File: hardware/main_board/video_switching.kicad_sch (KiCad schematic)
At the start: 33 parts, among them SW1 rgb/ypbpr, SW2 rgb/ypbpr, SW3 rgb/ypbpr, SW4 rgb/ypbpr, SW5 rgb/ypbpr, SW6 rgb/ypbpr, SW7 rgb/ypbpr, SW8 rgb/ypbpr, U10 SN74CBT3244CPW, U11 SN74CBT3244CPW, U12 SN74CBT3244CPW, U13 SN74CBT3244CPW, U14 74HC238, U15 74HC238, U3 SN74CBT3244CPW, U4 SN74CBT3244CPW, U5 74HC138, U6 74HC04, U7 SN74CBT3244CPW, U8 SN74CBT3244CPW, U9 SN74CBT3244CPW

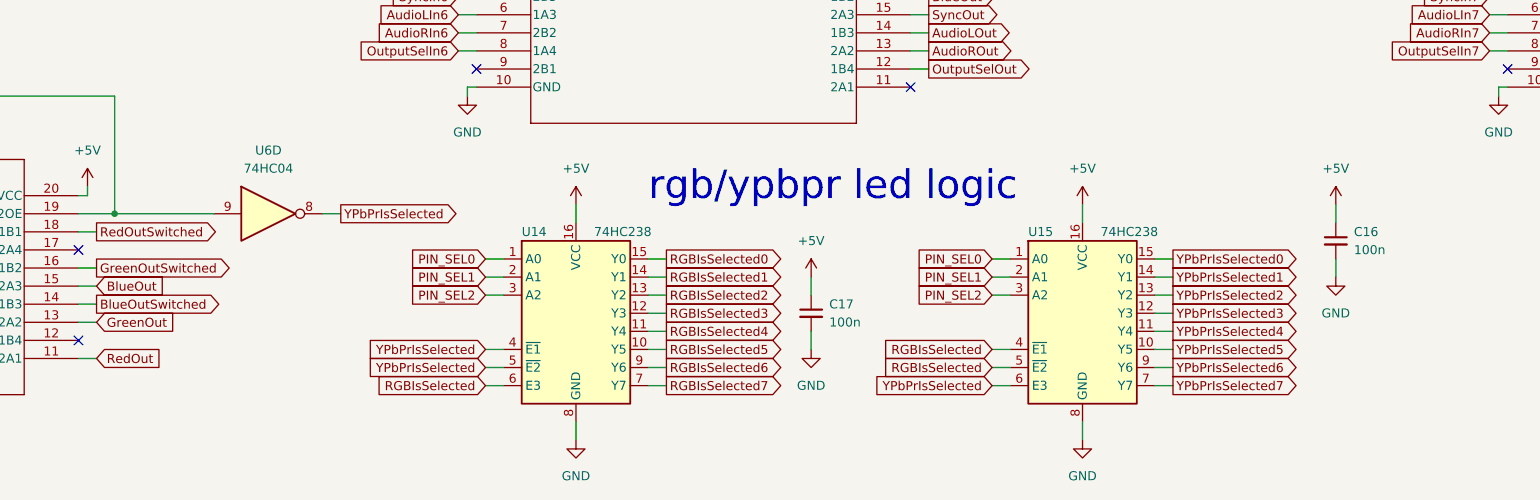
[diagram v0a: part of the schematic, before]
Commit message: #2: Hardware changes to accommodate new standby feature. Might as well commit symbol/footprint tables.
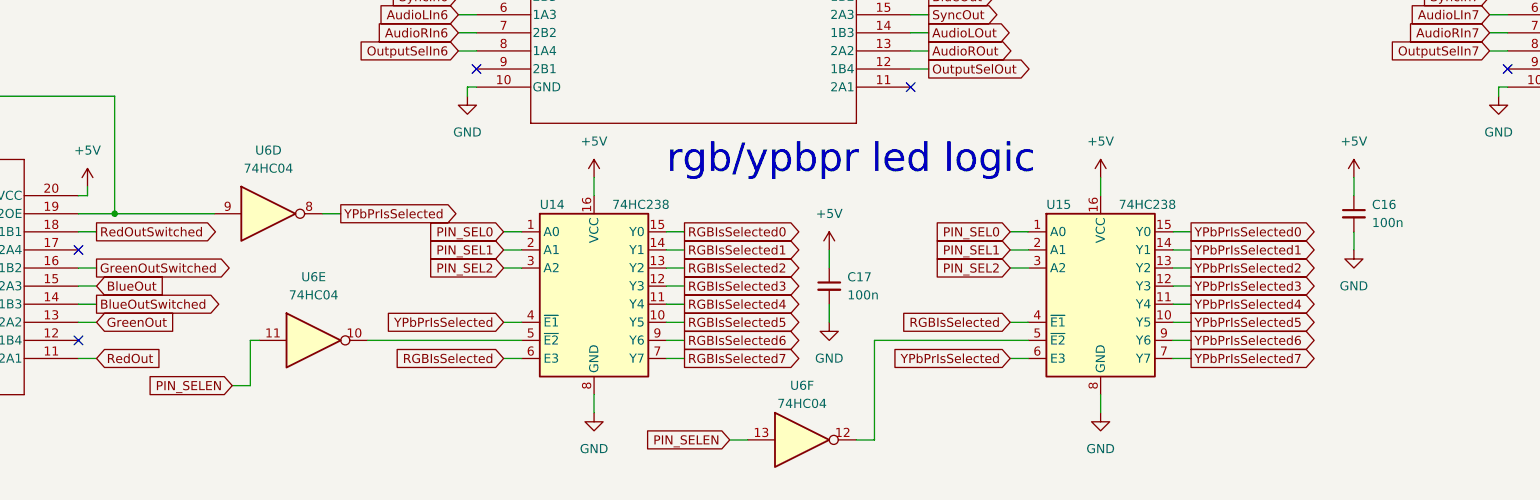
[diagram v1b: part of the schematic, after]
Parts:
- added unit 5 of U6
- added unit 6 of U6
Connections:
- net OutputSelOut: no longer U15.5 (~{E2})
- net PIN_SELEN: now also U6.11, U6.13
- net YPbPrIsSelected: no longer U14.5 (~{E2})
- new net: U14.5 (~{E2}), U6.10
- new net: U15.5 (~{E2}), U6.12
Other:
- moved on the sheet: C16, C17, U14, U15

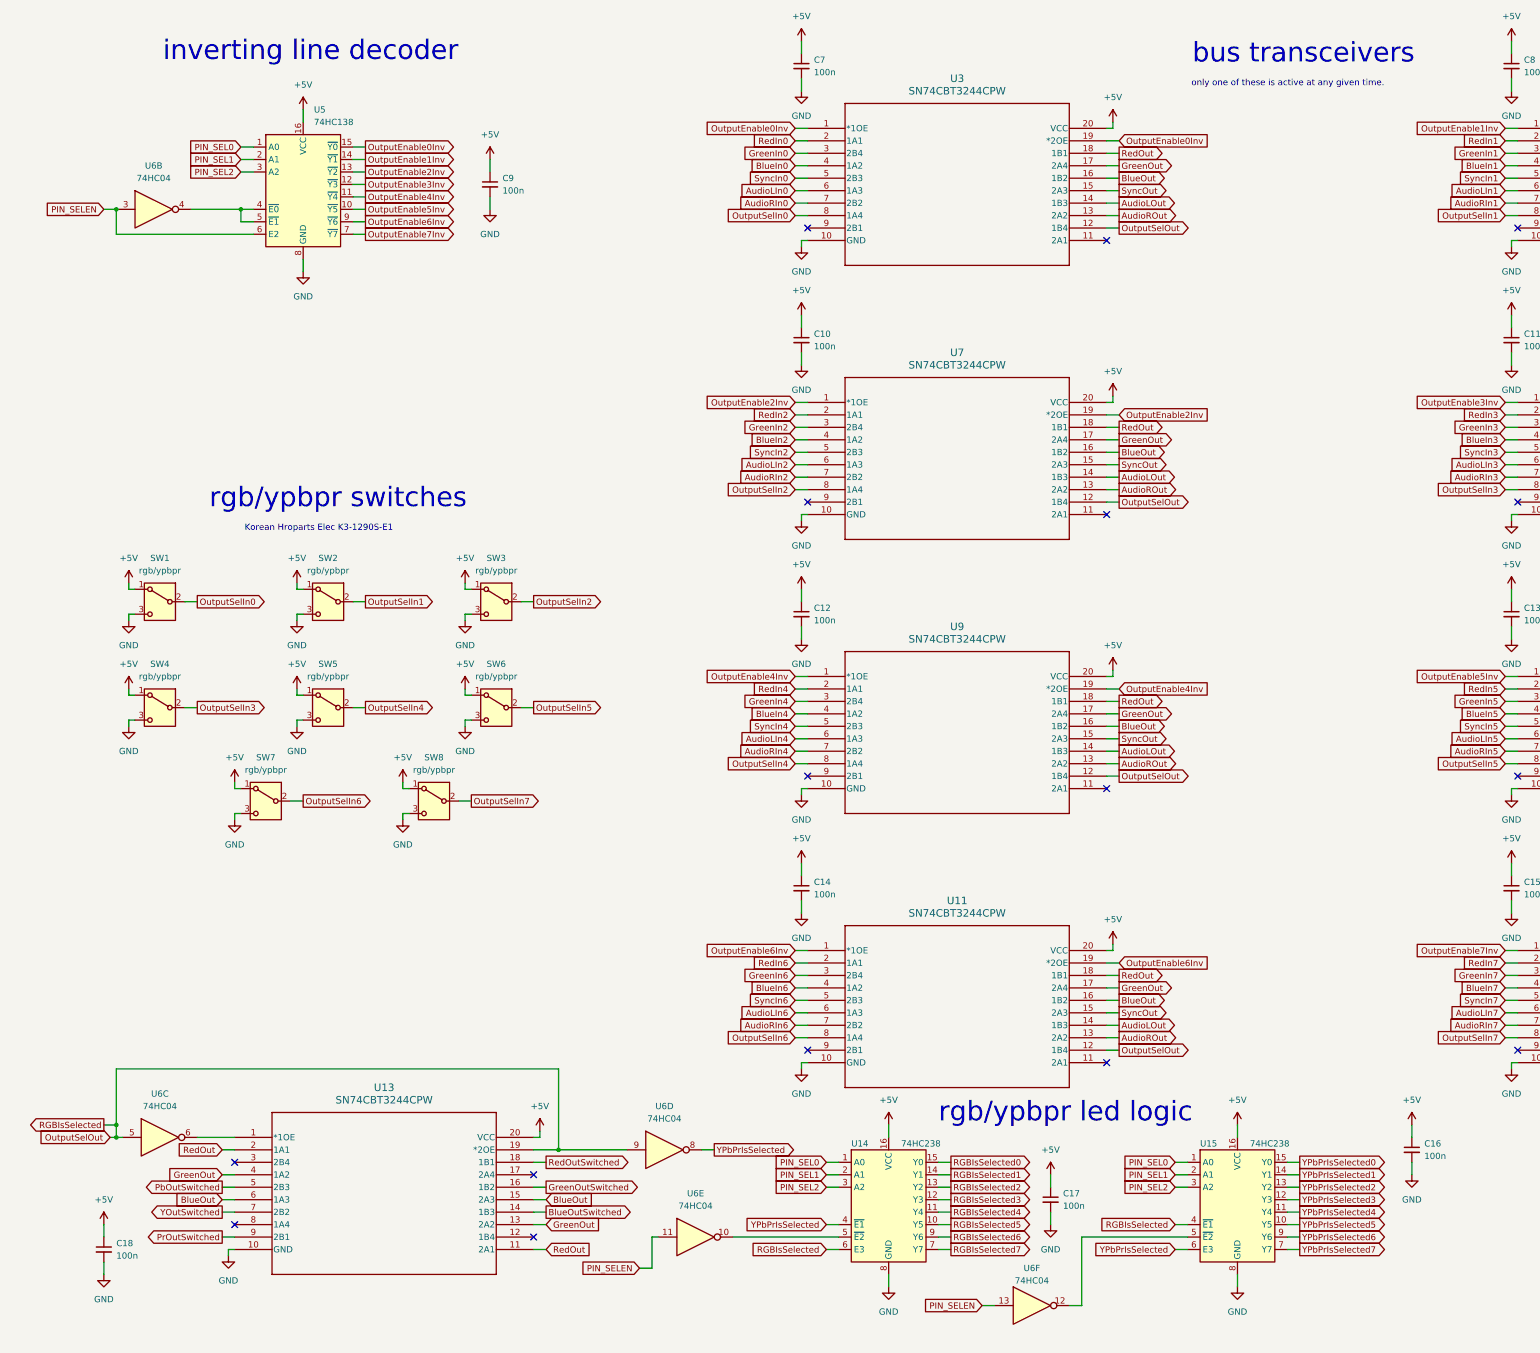
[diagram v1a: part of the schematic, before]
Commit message: #5: Removed LED-related things from main_board. Replaced power inlet with USB-C connector configured to accept 5V. Not sure what current consumption will be like though...
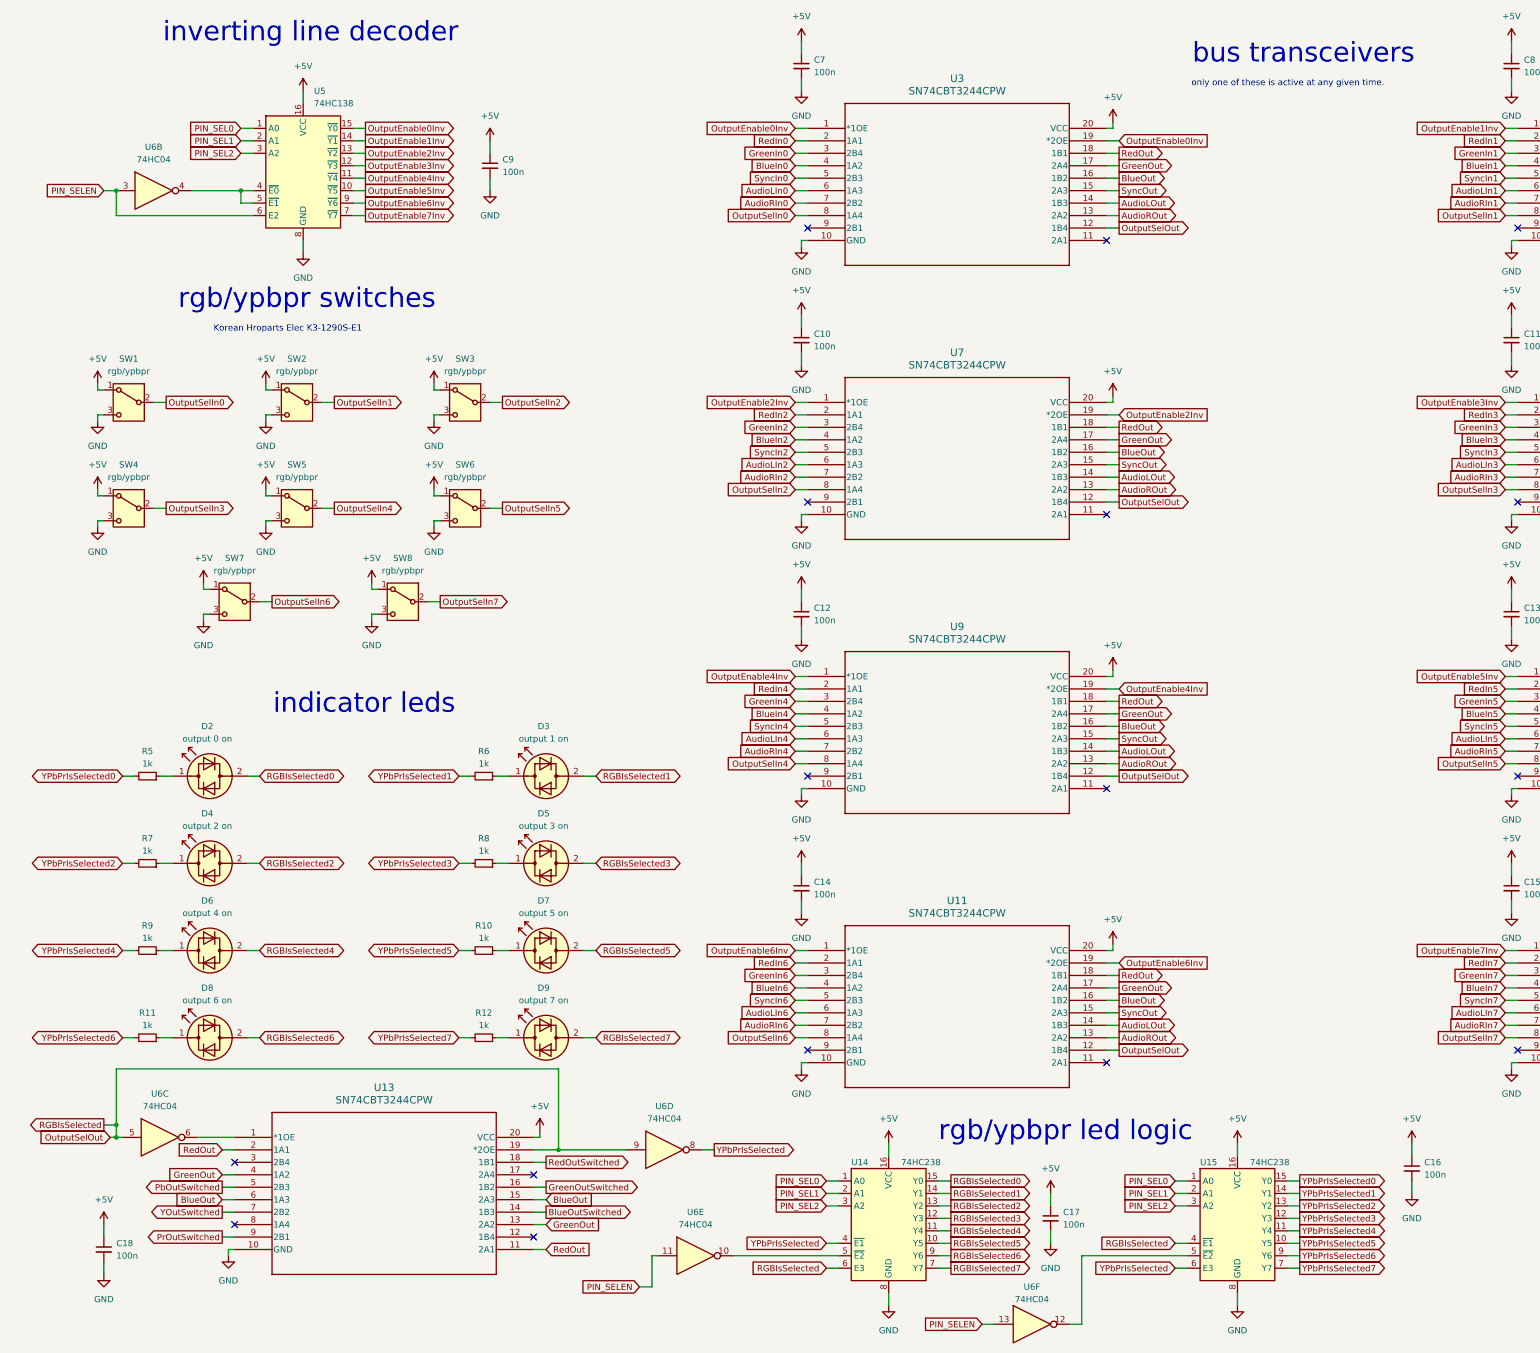
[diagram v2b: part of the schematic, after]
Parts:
- added D2: output 0 on, LED_THT:LED_D5.0mm, symbol Device:LED_Dual_Bidirectional
- added D3: output 1 on, LED_THT:LED_D5.0mm, symbol Device:LED_Dual_Bidirectional
- added D4: output 2 on, LED_THT:LED_D5.0mm, symbol Device:LED_Dual_Bidirectional
- added D5: output 3 on, LED_THT:LED_D5.0mm, symbol Device:LED_Dual_Bidirectional
- added D6: output 4 on, LED_THT:LED_D5.0mm, symbol Device:LED_Dual_Bidirectional
- added D7: output 5 on, LED_THT:LED_D5.0mm, symbol Device:LED_Dual_Bidirectional
- added D8: output 6 on, LED_THT:LED_D5.0mm, symbol Device:LED_Dual_Bidirectional
- added D9: output 7 on, LED_THT:LED_D5.0mm, symbol Device:LED_Dual_Bidirectional
- added R10, R11, R12, R5, R6, R7, R8, R9: 1k, Resistor_SMD:R_0603_1608Metric, symbol Device:R_Small
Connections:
- net RGBIsSelected0: now also D2.2 (AK)
- net RGBIsSelected1: now also D3.2 (AK)
- net RGBIsSelected2: now also D4.2 (AK)
- net RGBIsSelected3: now also D5.2 (AK)
- net RGBIsSelected4: now also D6.2 (AK)
- net RGBIsSelected5: now also D7.2 (AK)
- net RGBIsSelected6: now also D8.2 (AK)
- net RGBIsSelected7: now also D9.2 (AK)
- net YPbPrIsSelected0: now also R5.2
- net YPbPrIsSelected1: now also R6.2
- net YPbPrIsSelected2: now also R7.2
- net YPbPrIsSelected3: now also R8.2
- net YPbPrIsSelected4: now also R9.2
- net YPbPrIsSelected5: now also R10.2
- net YPbPrIsSelected6: now also R11.2
- net YPbPrIsSelected7: now also R12.2
- new net: D3.1 (KA), R6.1
- new net: D7.1 (KA), R10.1
- new net: D9.1 (KA), R12.1
- new net: D6.1 (KA), R9.1
- new net: D2.1 (KA), R5.1
- new net: D8.1 (KA), R11.1
- new net: D4.1 (KA), R7.1
- new net: D5.1 (KA), R8.1
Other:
- note added: "indicator leds"
- moved on the sheet: C16, C17, C9, SW1, SW2, SW3, SW4, SW5, SW6, SW7, SW8, U14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

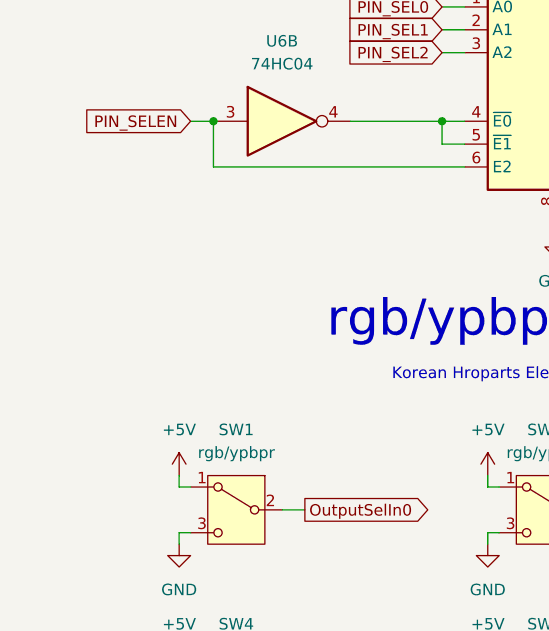
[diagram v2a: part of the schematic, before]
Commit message: #5: Honey, I shrunk the board! It's now 135x226mm and devoid of LED-related things.
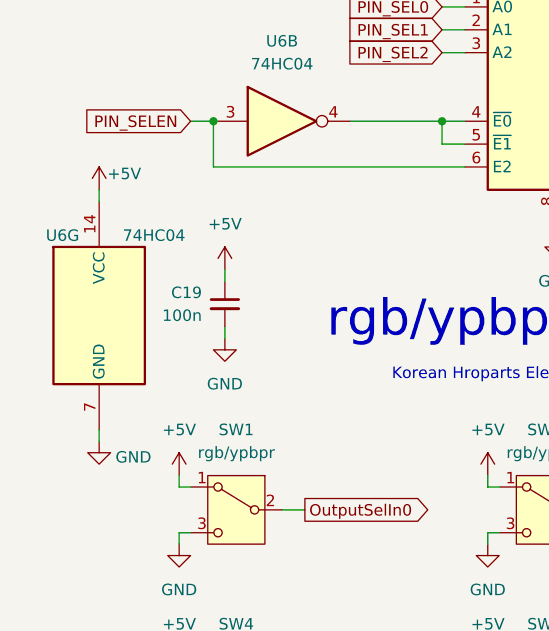
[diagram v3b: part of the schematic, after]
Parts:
- added C19: 100n, Capacitor_SMD:C_0603_1608Metric, symbol Device:C_Small
- added unit 7 of U6
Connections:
- net +5V: now also C19.1, U6.14 (VCC)
- net GND: now also C19.2, U6.7 (GND)

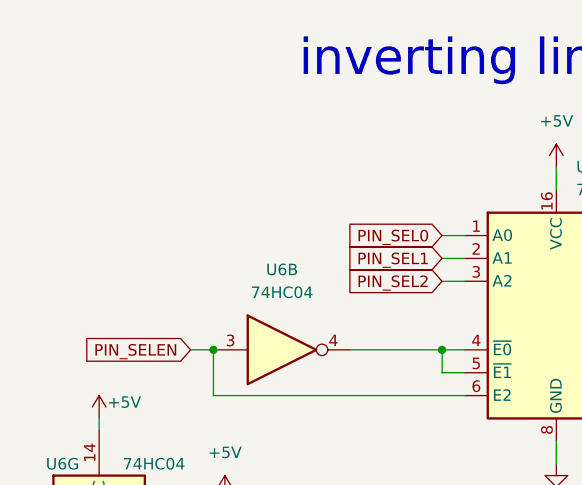
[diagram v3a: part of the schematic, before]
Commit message: #5: Properly handle unused NOT gate. Prune unused symbol/footprint libs.
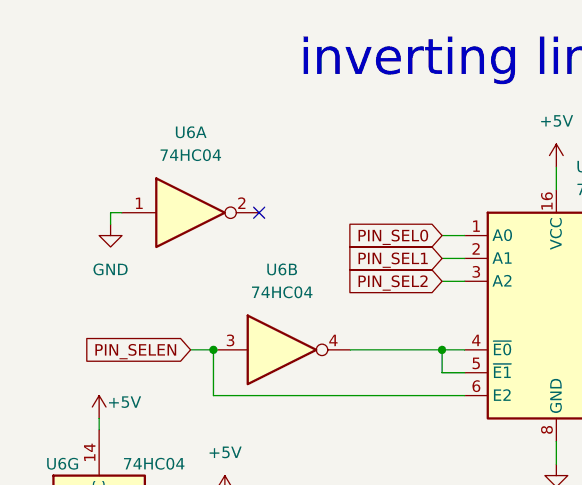
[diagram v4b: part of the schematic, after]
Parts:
- added unit 1 of U6
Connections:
- net GND: now also U6.1
- no-connect marks 20 -> 21
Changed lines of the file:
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@@
 		(at 173.99 168.91)
 	)
+	(no_connect
+		(at 38.1 34.29)
+	)
 	(wire
 		(pts
@@
 	(wire
 		(pts
+			(xy 22.86 34.29) (xy 21.59 34.29)
+		)
+		(stroke
+			(width 0)
+			(type default)
+		)
+	)
+	(wire
+		(pts
 			(xy 118.11 247.65) (xy 120.65 247.65)
 		)
@@
 		)
 	)
+	(wire
+		(pts
+			(xy 21.59 34.29) (xy 21.59 35.56)
+		)
+		(stroke
+			(width 0)
+			(type default)
+		)
+	)
 	(global_label "SyncIn7"
 		(shape input)
@@
 	)
 	(symbol
+		(lib_id "power:GND")
+		(at 21.59 35.56 0)
+		(unit 1)
+		(exclude_from_sim no)
+		(in_bom yes)
+		(on_board yes)
+		(dnp no)
+		(fields_autoplaced yes)
+		(property "Reference" "#PWR0110"
+			(at 21.59 41.91 0)
+			(effects
+				(font
+					(size 1.27 1.27)
+				)
+				(hide yes)
+			)
+		)
+		(property "Value" "GND"
+			(at 21.59 40.64 0)
+			(effects
+				(font
+					(size 1.27 1.27)
+				)
+			)
+		)
+		(property "Footprint" ""
+			(at 21.59 35.56 0)
+			(effects
+				(font
+					(size 1.27 1.27)
+				)
+				(hide yes)
+			)
+		)
+		(property "Datasheet" ""
+			(at 21.59 35.56 0)
+			(effects
+				(font
+					(size 1.27 1.27)
+				)
+				(hide yes)
+			)
+		)
+		(property "Description" "Power symbol creates a global label with name \"GND\" , ground"
+			(at 21.59 35.56 0)
+			(effects
+				(font
+					(size 1.27 1.27)
+				)
+				(hide yes)
+			)
+		)
+		(pin "1"
+		)
+		(instances
+			(project "main_board"
+				(path "/d2c111d0-ce33-4895-b1f4-02ad9d9e0b8d/8928c934-163b-4780-a91c-52d031c71614"
+					(reference "#PWR0110")
+					(unit 1)
+				)
+			)
+		)
+	)
+	(symbol
 		(lib_id "power:+5V")
 		(at 29.21 88.9 0)
@@
 					(unit 1)
 				)
+			)
+		)
+	)
+	(symbol
+		(lib_id "74xx:74HC04")
+		(at 30.48 34.29 0)
+		(unit 1)
+		(exclude_from_sim no)
+		(in_bom yes)
+		(on_board yes)
+		(dnp no)
+		(fields_autoplaced yes)
+		(property "Reference" "U6"
+			(at 30.48 25.4 0)
+			(effects
+				(font
+					(size 1.27 1.27)
+				)
+			)
+		)
+		(property "Value" "74HC04"
+			(at 30.48 27.94 0)
+			(effects
+				(font
+					(size 1.27 1.27)
+				)
+			)
+		)
+		(property "Footprint" "Package_SO:SOIC-14_3.9x8.7mm_P1.27mm"
+			(at 30.48 34.29 0)
+			(effects
+				(font
+					(size 1.27 1.27)
+				)
+				(hide yes)
+			)
+		)
+		(property "Datasheet" "https://assets.nexperia.com/documents/data-sheet/74HC_HCT04.pdf"
+			(at 30.48 34.29 0)
+			(effects
+				(font
+					(size 1.27 1.27)
+				)
+				(hide yes)
+			)
+		)
+		(property "Description" "Hex Inverter"
+			(at 30.48 34.29 0)
+			(effects
+				(font
+					(size 1.27 1.27)
+				)
+				(hide yes)
+			)
+		)
+		(pin "1"
+		)
+		(pin "9"
+		)
+		(pin "10"
+		)
+		(pin "6"
+		)
+		(pin "8"
+		)
+		(pin "4"
+		)
+		(pin "5"
+		)
+		(pin "3"
+		)
+		(pin "14"
+		)
+		(pin "2"
+		)
+		(pin "11"
+		)
+		(pin "13"
+		)
+		(pin "12"
+		)
+		(pin "7"
+		)
+		(instances
+			(project "main_board"
+				(path "/d2c111d0-ce33-4895-b1f4-02ad9d9e0b8d/8928c934-163b-4780-a91c-52d031c71614"
+					(reference "U6")
+					(unit 1)
+				)
